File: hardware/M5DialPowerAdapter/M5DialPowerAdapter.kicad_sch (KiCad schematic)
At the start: 15 parts, among them J1 Power In, J2 LED Power, J3 M5Dial Power, J4 JST XH I2C, J5 Grove I2C, U1 AMS1117-3.3

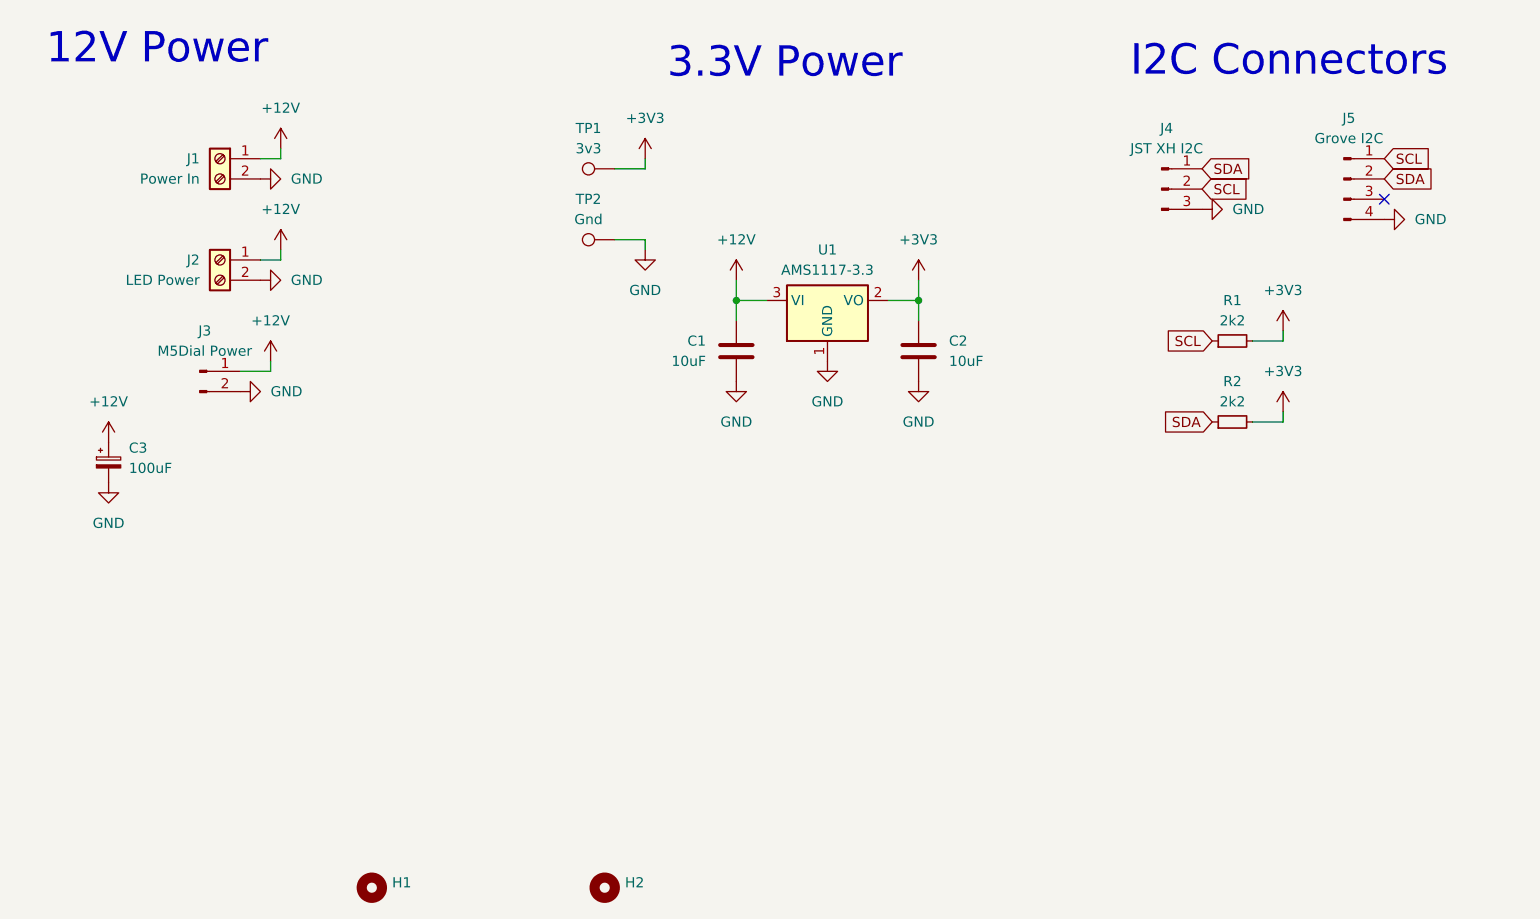
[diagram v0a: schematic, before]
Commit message: Updates to bring 12 volts from Caddy
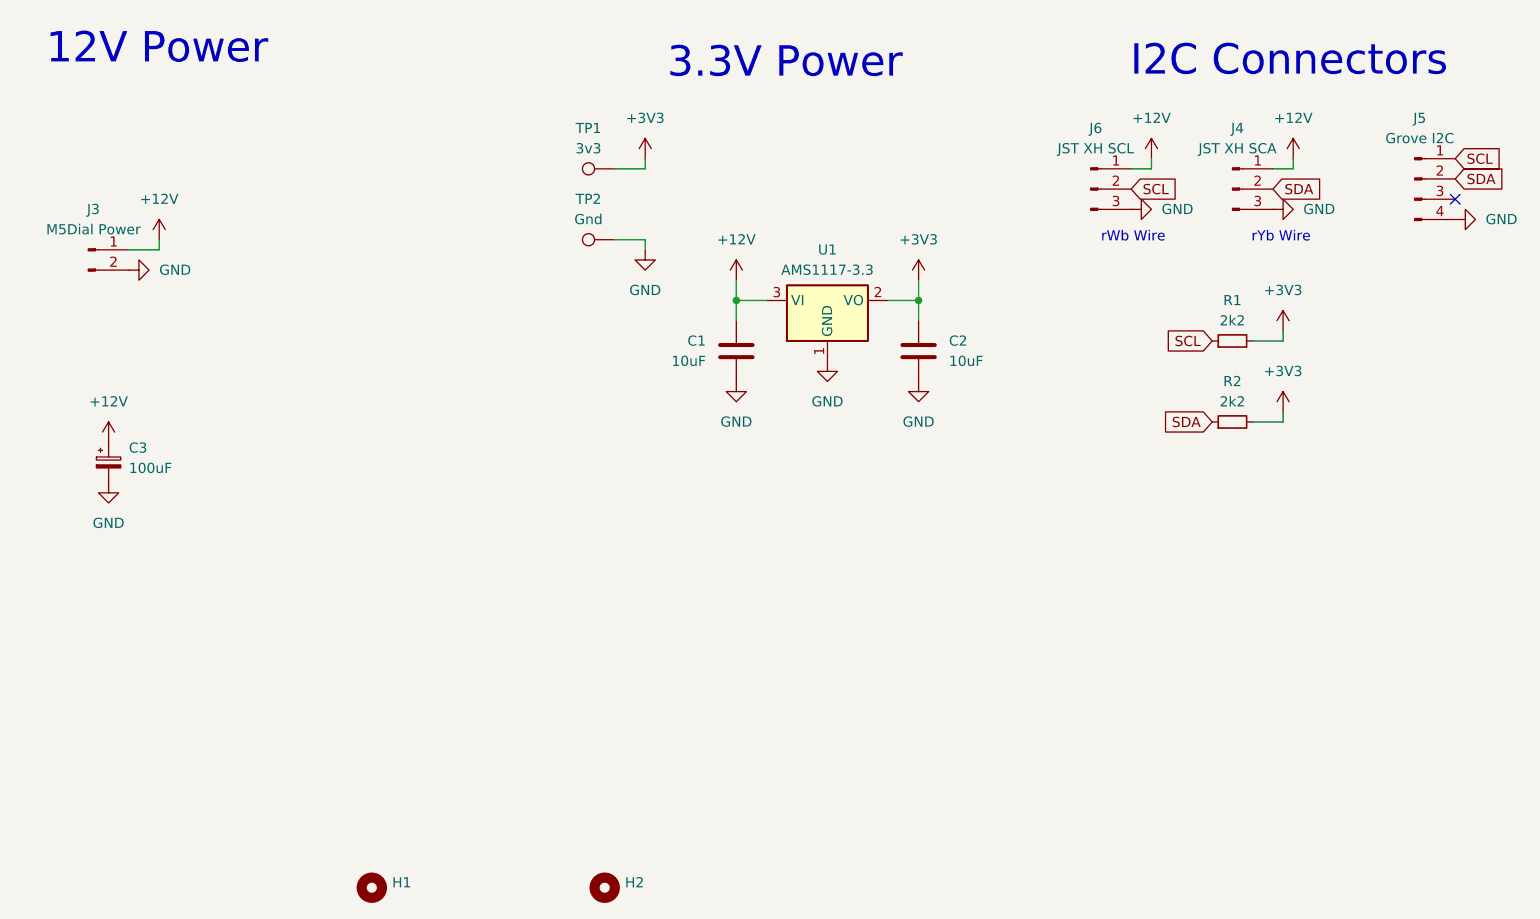
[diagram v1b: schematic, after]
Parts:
- removed J1: Power In, Useful Modifications:TerminalBlock_bornier-2_P5.08mm, symbol Connector:Screw_Terminal_01x02
- removed J2: LED Power, Useful Modifications:TerminalBlock_bornier-2_P5.08mm, symbol Connector:Screw_Terminal_01x02
- added J6: JST XH SCL, Connector_JST:JST_XH_B3B-XH-A_1x03_P2.50mm_Vertical, symbol Connector:Conn_01x03_Pin
- J4: value JST XH I2C -> JST XH SCA
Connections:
- net +12V: now also J4.1 (Pin_1), J6.1 (Pin_1)
- net GND: now also J6.3 (Pin_3)
- net SCL: now also J6.2 (Pin_2); no longer J4.2 (Pin_2)
- net SDA: now also J4.2 (Pin_2); no longer J4.1 (Pin_1)
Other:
- note added: "rWb Wire"
- note added: "rYb Wire"
- moved on the sheet: J3, J4, J5
